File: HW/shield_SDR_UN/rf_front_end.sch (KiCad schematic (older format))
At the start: 69 parts, among them Q1 MOSFET_P, U1 MAX5864, U2 MAX2830

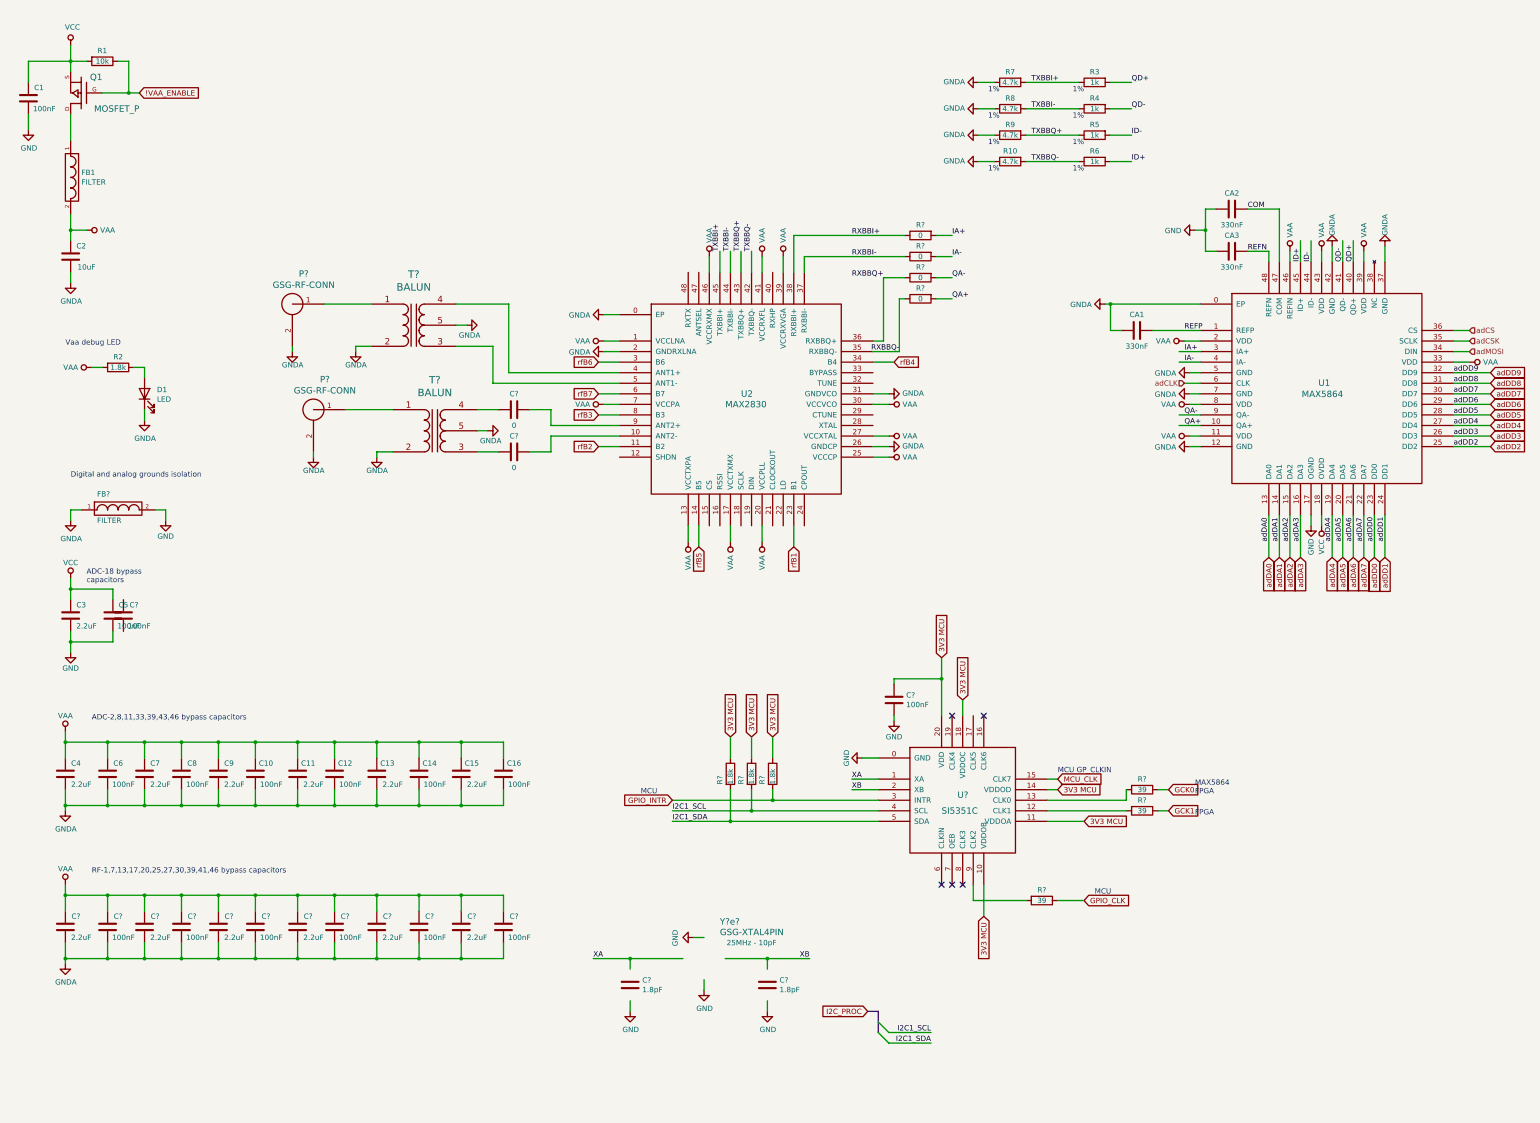
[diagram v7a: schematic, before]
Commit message: Footprints added for C and R
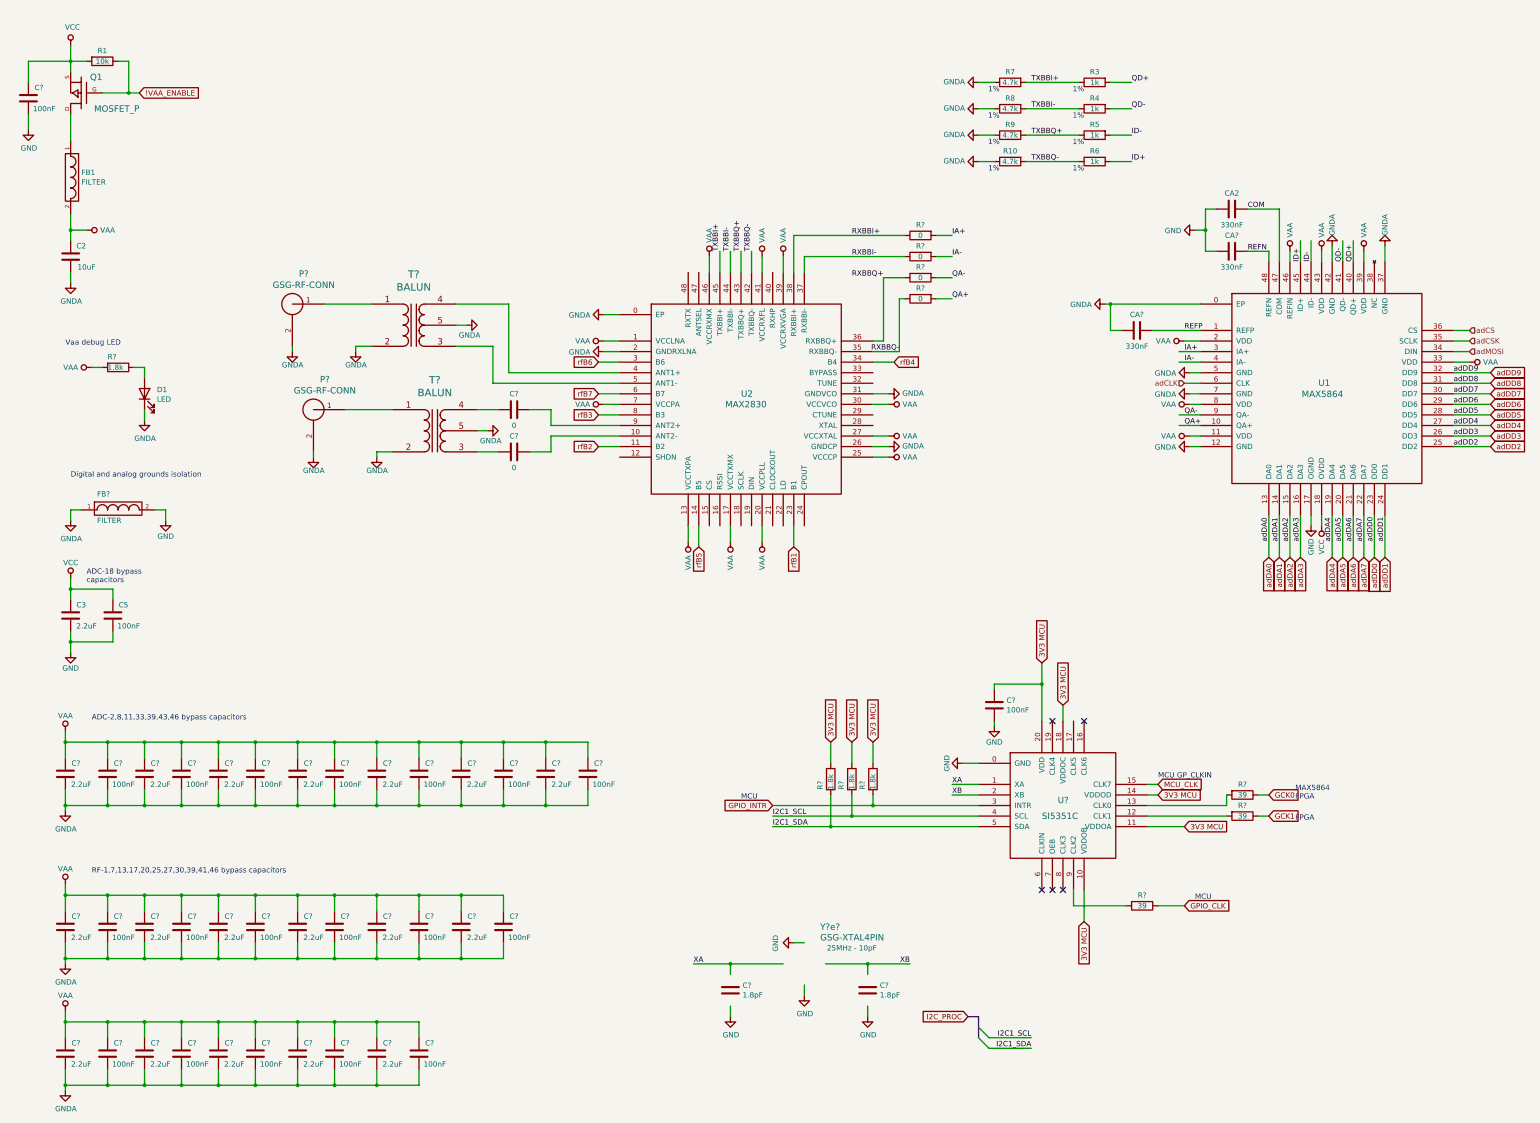
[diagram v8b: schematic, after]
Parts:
- removed C1, C10, C12, C14, C16, C6, C8, C? (x7): 100nF, symbol Device:C
- removed C11, C13, C15, C4, C7, C9, C? (x6): 2.2uF, symbol Device:C
- removed CA1, CA3: 330nF, symbol Device:C
- removed R2: 1.8k, symbol Device:R
- removed R? (x2): 1.8k, Resistor_SMD:R_0603_1608Metric_Pad1.05x0.95mm_HandSolder, symbol Device:R
- added C? (x19): 100nF, Capacitor_SMD:C_0603_1608Metric_Pad1.05x0.95mm_HandSolder, symbol Device:C
- added C? (x18): 2.2uF, Capacitor_SMD:C_0603_1608Metric_Pad1.05x0.95mm_HandSolder, symbol Device:C
- added CA? (x2): 330nF, Capacitor_SMD:C_0603_1608Metric_Pad1.05x0.95mm_HandSolder, symbol Device:C
- added R? (x3): 1.8k, Resistor_SMD:R_0603_1608Metric_Pad1.05x0.95mm_HandSolder, symbol Device:R
- C2: footprint (none) -> Capacitor_SMD:C_0805_2012Metric_Pad1.15x1.40mm_HandSolder; Digikey (none) -> 1276-6456-1-ND
- C3: footprint (none) -> Capacitor_SMD:C_0603_1608Metric_Pad1.05x0.95mm_HandSolder; Digikey (none) -> 1276-1183-1-ND
- C5: footprint (none) -> Capacitor_SMD:C_0603_1608Metric_Pad1.05x0.95mm_HandSolder; Digikey (none) -> 1276-1000-1-ND
- CA2: footprint (none) -> Capacitor_SMD:C_0603_1608Metric_Pad1.05x0.95mm_HandSolder; Digikey (none) -> 1276-2048-1-ND
- R?: Digikey (none) -> 311-1.8KGRTR-ND
- U?: footprint (none) -> QFN50P300X300X60-21N:QFN50P300X300X60-21N; Digikey (none) -> 336-5160-1-ND
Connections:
- wire segments 306 -> 354
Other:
- moved on the sheet: C?, R?, U?
